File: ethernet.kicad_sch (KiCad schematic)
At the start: 22 parts, among them J2 L834-1G1T-S7, Q2 PMOS_Substrate, U2 LAN8830T_PSA

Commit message: Start of ethernet
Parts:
- removed J2: L834-1G1T-S7, L834-1G1T-S7:BEL_L834-1G1T-S7, symbol Library:L834-1G1T-S7
- removed U2: LAN8830T_PSA, LAN8830T_PSA:QFN50P700X700X100-49N, symbol Library:LAN8830T_PSA
- added J2: ARJM11B1-502-AB-EW2, Library:ABRACON_ARJM11B1-502-AB-EW2, symbol Library:ARJM11B1-502-AB-EW2
- added R11, R12: 100, symbol Device:R_Small_US
- added R2, R6: 75, symbol Device:R_Small_US
- added U2: MXL86110C-AQB-R, QFN40_5X5_MXL, symbol Library:MXL86110C-AQB-R
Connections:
- net ETH_LED1: now also R11.2
- net ETH_LED2: now also R12.2
- net GND: now also J2.12, J2.14, R2.1, R6.1
- new net: J2.11, R11.1
- new net: J2.13, R12.1
- new net: J2.5 (CT), J2.6 (CT__1), R2.2, R6.2
- new net TD1+: J2.1 (TD1+), U2.1 (TPIAP)
- new net TD1-: J2.2 (TD1-), U2.2 (TPIAN)
- new net TD2+: J2.3 (TD2+), U2.4 (TPIBP)
- new net TD2-: J2.4 (TD2-), U2.5 (TPIBN)
- new net TD3+: J2.7 (TD3+), U2.6 (TPICP)
- new net TD3-: J2.8 (TD3-), U2.7 (TPICN)
- new net TD4+: J2.9 (TD4+), U2.9 (TPIDP)
- new net TD4-: J2.10 (TD4-), U2.10 (TPIDN)
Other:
- moved on the sheet: L1, L2

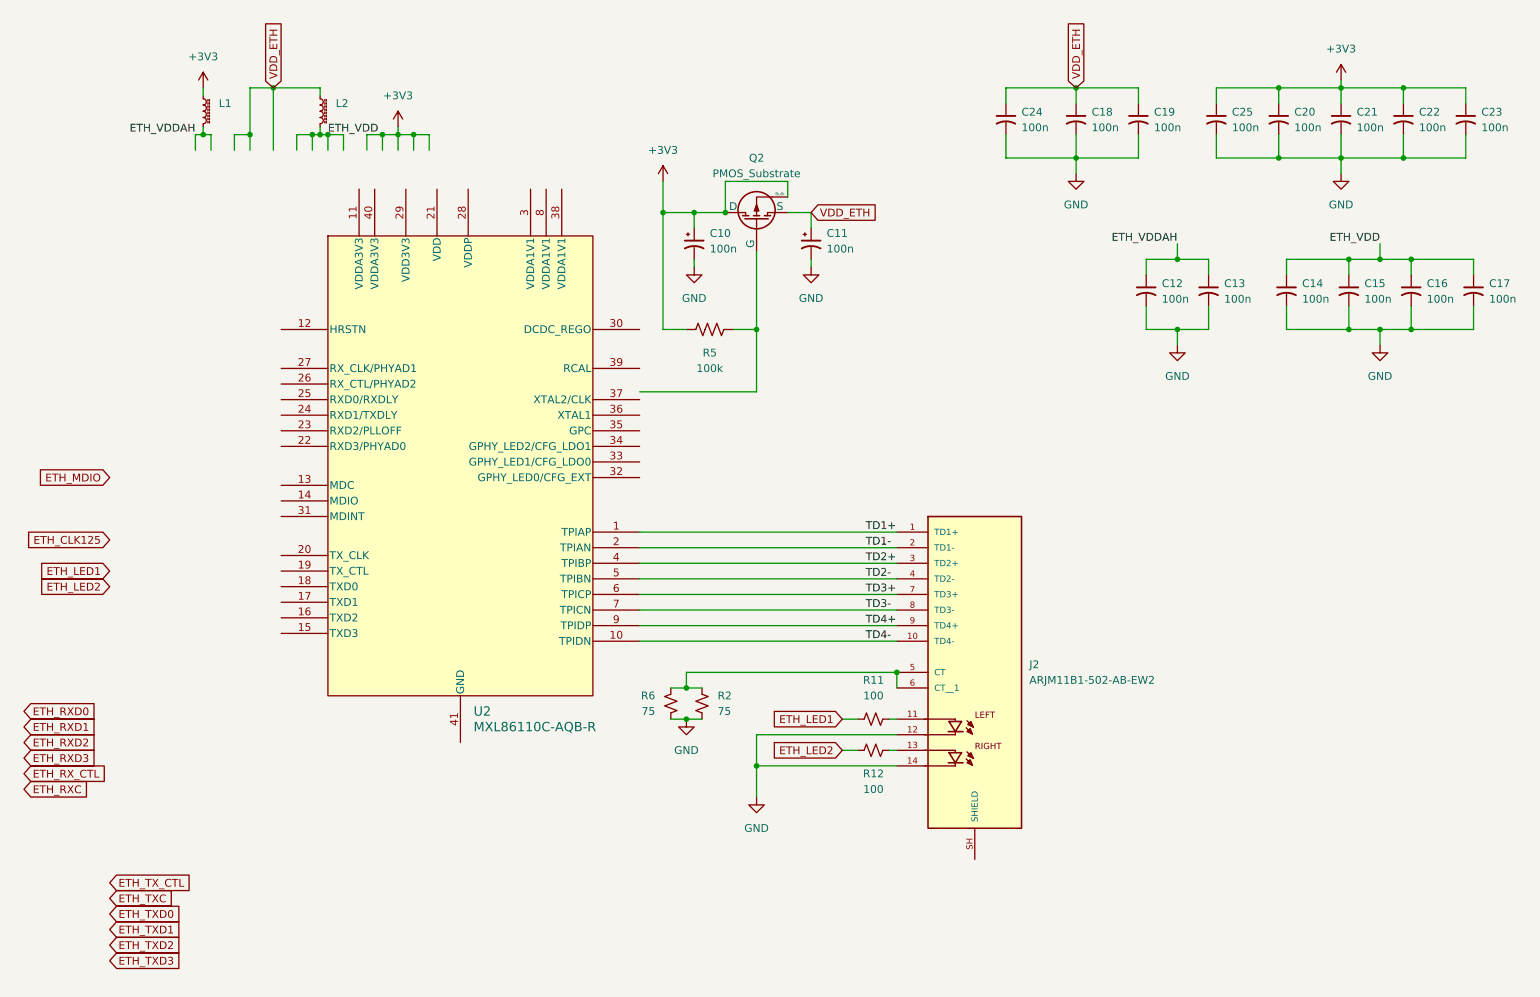
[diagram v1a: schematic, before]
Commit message: Ethernet schematic done
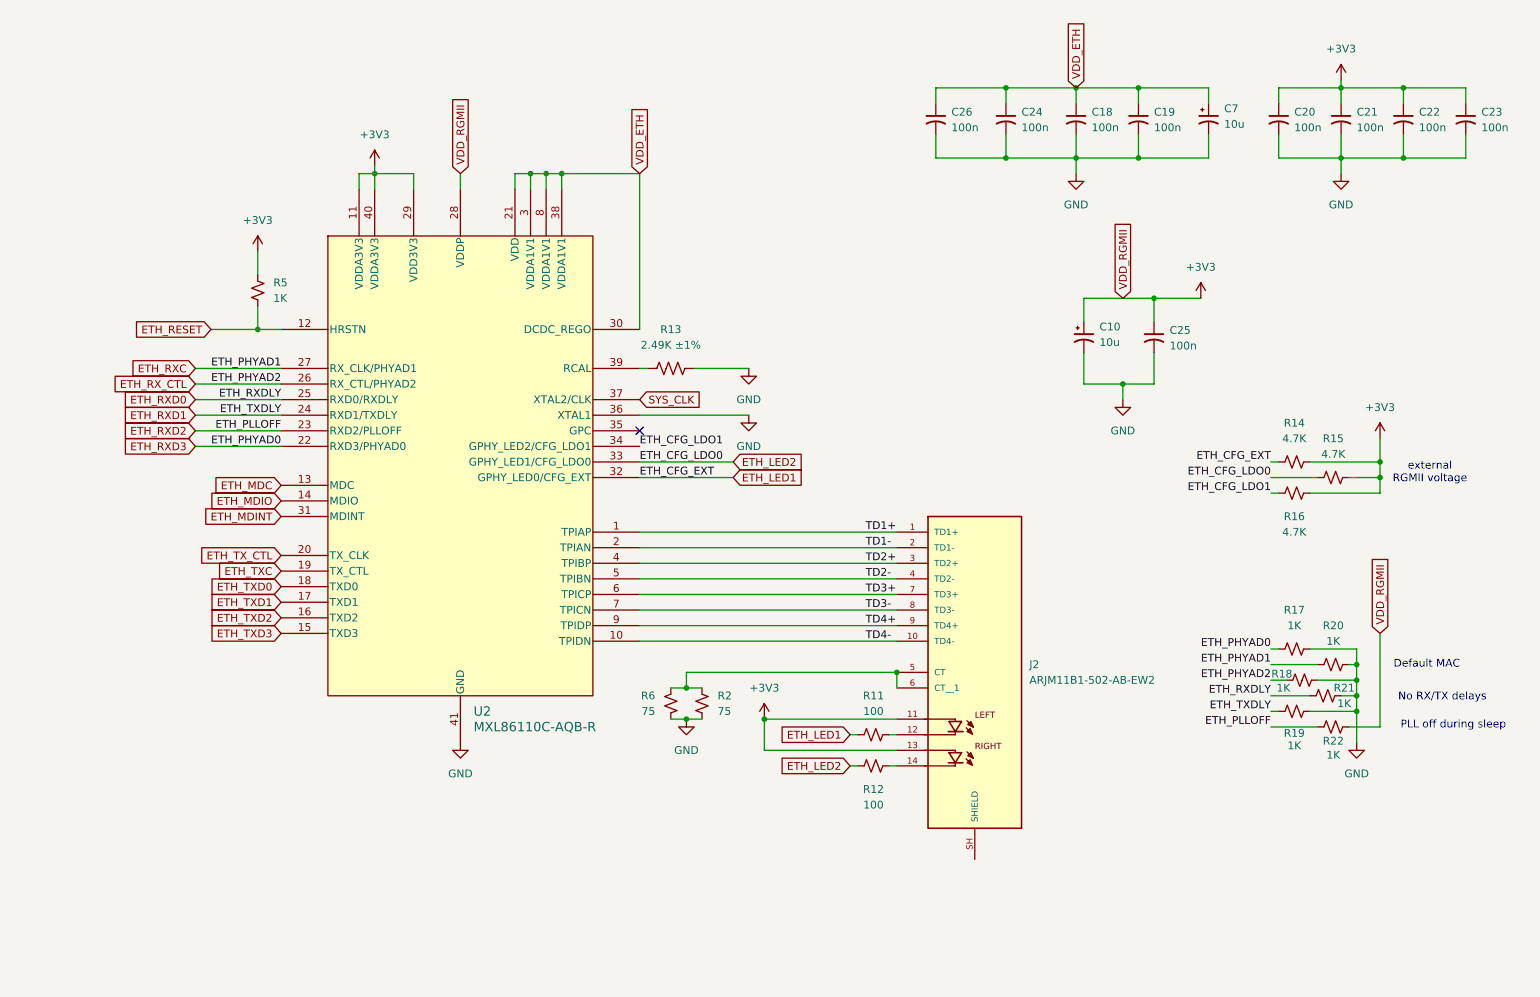
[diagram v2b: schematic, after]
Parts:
- removed C11: 100n, symbol Device:C_Polarized_Small_US
- removed C12, C13, C14, C15, C16, C17: 100n, symbol Device:C_Small_US
- removed L1, L2: L_Ferrite_Small, symbol Device:L_Ferrite_Small
- removed Q2: PMOS_Substrate, symbol Simulation_SPICE:PMOS_Substrate
- removed R5: 100k, symbol Device:R_US
- added C26: 100n, Capacitor_SMD:C_0402_1005Metric, symbol Device:C_Small_US
- added C7: 10u, Capacitor_Tantalum_SMD:CP_EIA-3216-12_Kemet-S, symbol Device:C_Polarized_Small_US
- added R13: 2.49K ±1%, Resistor_SMD:R_0402_1005Metric, symbol Device:R_US
- added R14, R15, R16: 4.7K, Capacitor_SMD:C_0402_1005Metric, symbol Device:R_Small_US
- added R17, R18, R19, R20, R21, R22, R5: 1K, Capacitor_SMD:C_0402_1005Metric, symbol Device:R_Small_US
- C10: value 100n -> 10u; footprint (none) -> Capacitor_Tantalum_SMD:CP_EIA-3216-12_Kemet-S
- C18, C19, C20, C21, C22, C23, C24, C25, R11, R12, R2, R6: footprint (none) -> Capacitor_SMD:C_0402_1005Metric
- U2: footprint QFN40_5X5_MXL -> Library:QFN40_5X5_MXL
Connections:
- net +3V3: now also J2.11, J2.13, U2.11 (VDDA3V3), U2.28 (VDDP), U2.29 (VDD3V3), U2.40 (VDDA3V3), R14.1, R15.1, R16.1, R22.1, R5.2
- net ETH_LED1: now also U2.32 (GPHY_LED0/CFG_EXT), R14.2
- net ETH_LED2: now also U2.33 (GPHY_LED1/CFG_LDO0), R15.2
- net ETH_MDIO: now also U2.14 (MDIO)
- net ETH_RXC: now also U2.27 (RX_CLK/PHYAD1), R20.2
- net ETH_RXD0: now also U2.25 (RXD0/RXDLY), R21.2
- net ETH_RXD1: now also U2.24 (RXD1/TXDLY), R19.2
- net ETH_RXD2: now also U2.23 (RXD2/PLLOFF), R22.2
- net ETH_RXD3: now also U2.22 (RXD3/PHYAD0), R17.2
- net ETH_RX_CTL: now also U2.26 (RX_CTL/PHYAD2), R18.2
- net ETH_TXC: now also U2.19 (TX_CTL)
- net ETH_TXD0: now also U2.18 (TXD0)
- net ETH_TXD1: now also U2.17 (TXD1)
- net ETH_TXD2: now also U2.16 (TXD2)
- net ETH_TXD3: now also U2.15 (TXD3)
- net ETH_TX_CTL: now also U2.20 (TX_CLK)
- net GND: now also U2.36 (XTAL1), U2.41 (GND), C26.2, C7.2, R13.2, R17.1, R18.1, R19.1, R20.1, R21.1; no longer J2.12, J2.14
- net VDD_ETH: now also U2.21 (VDD), U2.3 (VDDA1V1), U2.30 (DCDC_REGO), U2.38 (VDDA1V1), U2.8 (VDDA1V1), C26.1, C7.1
- net at R11.1: now also J2.12; no longer J2.11
- net at R12.1: now also J2.14; no longer J2.13
- net ETH_RESET: now reaches U2.12 (HRSTN)
- net ETH_RESET: now also R5.1
- net ETH_MDC: now reaches U2.13 (MDC)
- net ETH_MDINT: now reaches U2.31 (MDINT)
- net ETH_CFG_LDO1: now reaches U2.34 (GPHY_LED2/CFG_LDO1)
- net ETH_CFG_LDO1: now also R16.2
- net SYS_CLK: now reaches U2.37 (XTAL2/CLK)
- net at U2.39 (RCAL): now also R13.1
- no-connect marks 0 -> 1
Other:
- note added: "Default MAC"
- note added: "No RX/TX delays"
- note added: "PLL off during sleep"
- note added: "external RGMII voltage"

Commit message: Base ethernet signals routed
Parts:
- J2: value ARJM11B1-502-AB-EW2 -> ARJM11D7-502-AB-EW2; footprint Library:ABRACON_ARJM11B1-502-AB-EW2 -> Library:ABRACON_ARJM11D7-502-AB-EW2

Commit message: Etherent MDI rerouted with correct trace widths
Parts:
- J2: value ARJM11D7-502-AB-EW2 -> TMJG0803HENL; footprint Library:ABRACON_ARJM11D7-502-AB-EW2 -> Library:RJ45_TMJG0803HENL
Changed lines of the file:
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@@
 			)
 		)
-		(property "Value" "ARJM11D7-502-AB-EW2"
+		(property "Value" "TMJG0803HENL"
 			(at 204.47 120.6499 0)
 			(show_name no)
@@
 			)
 		)
-		(property "Footprint" "Library:ABRACON_ARJM11D7-502-AB-EW2"
+		(property "Footprint" "Library:RJ45_TMJG0803HENL"
 			(at 195.58 119.38 0)
 			(hide yes)

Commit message: More PHY passives
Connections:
- net +3V3: now also R21.1
- net GND: no longer R21.1
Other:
- note added: "Delay RX CLK"
- note added: "No TX CLK delay"
- note removed: "No RX/TX delays"
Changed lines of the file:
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@@
 		)
 	)
-	(text "PLL off during sleep"
+	(text "No TX CLK delay\n"
 		(exclude_from_sim no)
-		(at 273.558 128.016 0)
+		(at 263.652 125.73 0)
 		(effects
 			(font
 				(size 1.27 1.27)
 			)
-		)
-	)
-	(text "No RX/TX delays"
+			(justify left)
+		)
+	)
+	(text "PLL off during sleep"
 		(exclude_from_sim no)
-		(at 271.78 123.444 0)
+		(at 273.558 128.27 0)
 		(effects
 			(font
 				(size 1.27 1.27)
 			)
+		)
+	)
+	(text "Delay RX CLK"
+		(exclude_from_sim no)
+		(at 263.652 123.19 0)
+		(effects
+			(font
+				(size 1.27 1.27)
+			)
+			(justify left)
 		)
 	)
@@
 	)
 	(junction
+		(at 261.62 123.19)
+		(diameter 0)
+		(color 0 0 0 0)
+	)
+	(junction
 		(at 257.81 118.11)
 		(diameter 0)
@@
 	(junction
 		(at 222.25 24.13)
-		(diameter 0)
-		(color 0 0 0 0)
-	)
-	(junction
-		(at 257.81 123.19)
 		(diameter 0)
 		(color 0 0 0 0)
@@
 	(wire
 		(pts
-			(xy 261.62 128.27) (xy 261.62 113.03)
+			(xy 261.62 128.27) (xy 261.62 123.19)
 		)
 		(stroke
@@
 	(wire
 		(pts
+			(xy 261.62 123.19) (xy 261.62 113.03)
+		)
+		(stroke
+			(width 0)
+			(type default)
+		)
+	)
+	(wire
+		(pts
 			(xy 123.19 38.1) (xy 125.73 38.1)
 		)
@@
 	(wire
 		(pts
-			(xy 257.81 120.65) (xy 257.81 123.19)
-		)
-		(stroke
-			(width 0)
-			(type default)
-		)
-	)
-	(wire
-		(pts
 			(xy 257.81 118.11) (xy 257.81 120.65)
 		)
@@
 	(wire
 		(pts
-			(xy 255.27 123.19) (xy 257.81 123.19)
-		)
-		(stroke
-			(width 0)
-			(type default)
-		)
-	)
-	(wire
-		(pts
 			(xy 243.84 120.65) (xy 246.38 120.65)
 		)
@@
 	(wire
 		(pts
+			(xy 255.27 123.19) (xy 261.62 123.19)
+		)
+		(stroke
+			(width 0)
+			(type default)
+		)
+	)
+	(wire
+		(pts
 			(xy 243.84 85.09) (xy 245.11 85.09)
 		)
@@
 	(wire
 		(pts
-			(xy 257.81 123.19) (xy 257.81 125.73)
-		)
-		(stroke
+			(xy 257.81 120.65) (xy 257.81 125.73)
+		)
+		(stroke

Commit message: More PHY passives
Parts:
- C10, C7: footprint Capacitor_Tantalum_SMD:CP_EIA-3216-12_Kemet-S -> Capacitor_Tantalum_SMD:CP_EIA-2012-12_Kemet-R
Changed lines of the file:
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@@
 			)
 		)
-		(property "Footprint" "Capacitor_Tantalum_SMD:CP_EIA-3216-12_Kemet-S"
+		(property "Footprint" "Capacitor_Tantalum_SMD:CP_EIA-2012-12_Kemet-R"
 			(at 213.36 64.77 0)
 			(hide yes)
@@
 			)
 		)
-		(property "Footprint" "Capacitor_Tantalum_SMD:CP_EIA-3216-12_Kemet-S"
+		(property "Footprint" "Capacitor_Tantalum_SMD:CP_EIA-2012-12_Kemet-R"
 			(at 233.68 29.21 0)
 			(hide yes)

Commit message: PHY RX routing and power
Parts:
- removed C21, C25: 100n, Capacitor_SMD:C_0402_1005Metric, symbol Device:C_Small_US
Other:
- moved on the sheet: C10, C23

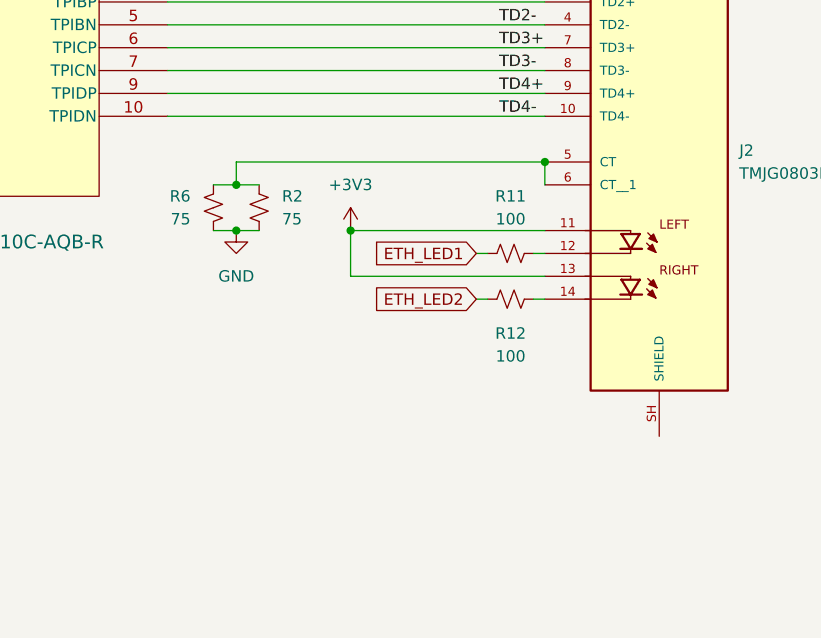
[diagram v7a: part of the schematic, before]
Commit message: Ethernet shielding
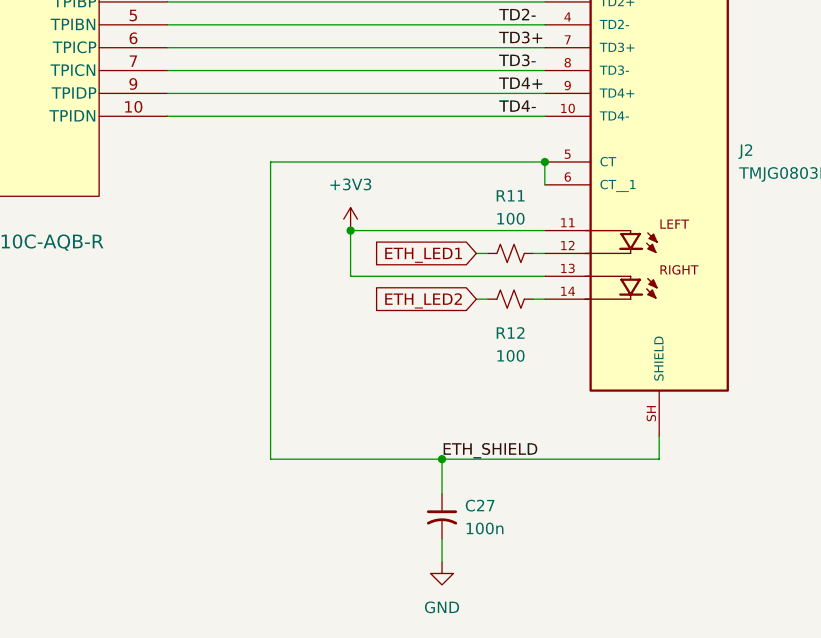
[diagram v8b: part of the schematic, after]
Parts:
- removed R2, R6: 75, Capacitor_SMD:C_0402_1005Metric, symbol Device:R_Small_US
- added C27: 100n, Capacitor_SMD:C_0402_1005Metric, symbol Device:C_Small_US
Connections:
- net GND: now also C27.2
- net ETH_SHIELD: now reaches J2.5 (CT), J2.6 (CT__1)
- net ETH_SHIELD: now also J2.SH (SHIELD), C27.1
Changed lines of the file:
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@@
 	)
 	(junction
-		(at 148.59 127)
-		(diameter 0)
-		(color 0 0 0 0)
-	)
-	(junction
 		(at 257.81 125.73)
 		(diameter 0)
@@
 	)
 	(junction
-		(at 261.62 87.63)
+		(at 171.45 152.4)
 		(diameter 0)
 		(color 0 0 0 0)
 	)
 	(junction
-		(at 148.59 121.92)
+		(at 261.62 87.63)
 		(diameter 0)
 		(color 0 0 0 0)
@@
 	(wire
 		(pts
-			(xy 148.59 127) (xy 151.13 127)
+			(xy 171.45 152.4) (xy 195.58 152.4)
 		)
 		(stroke
@@
 	(wire
 		(pts
+			(xy 152.4 152.4) (xy 152.4 119.38)
+		)
+		(stroke
+			(width 0)
+			(type default)
+		)
+	)
+	(wire
+		(pts
 			(xy 175.26 129.54) (xy 176.53 129.54)
 		)
@@
 	(wire
 		(pts
-			(xy 146.05 121.92) (xy 148.59 121.92)
+			(xy 171.45 163.83) (xy 171.45 161.29)
 		)
 		(stroke
@@
 	(wire
 		(pts
+			(xy 171.45 156.21) (xy 171.45 152.4)
+		)
+		(stroke
+			(width 0)
+			(type default)
+		)
+	)
+	(wire
+		(pts
 			(xy 233.68 26.67) (xy 233.68 24.13)
 		)
@@
 	(wire
 		(pts
+			(xy 152.4 152.4) (xy 171.45 152.4)
+		)
+		(stroke
+			(width 0)
+			(type default)
+		)
+	)
+	(wire
+		(pts
 			(xy 142.24 69.85) (xy 140.97 69.85)
 		)
@@
 	(wire
 		(pts
-			(xy 182.88 119.38) (xy 148.59 119.38)
+			(xy 182.88 119.38) (xy 152.4 119.38)
 		)
 		(stroke
@@
 	(wire
 		(pts
-			(xy 148.59 121.92) (xy 151.13 121.92)
-		)
-		(stroke
-			(width 0)
-			(type default)
-		)
-	)
-	(wire
-		(pts
 			(xy 261.62 85.09) (xy 261.62 81.28)
 		)
@@
 	(wire
 		(pts
-			(xy 148.59 119.38) (xy 148.59 121.92)
+			(xy 195.58 152.4) (xy 195.58 149.86)
 		)
 		(stroke
@@
 		)
 	)
-	(wire
-		(pts
-			(xy 146.05 127) (xy 148.59 127)
-		)
-		(stroke
-			(width 0)
-			(type default)
-		)
-	)
 	(label "VDD_RGMII"
 		(at 111.76 38.1 90)
@@
 		)
 	)
+	(label "ETH_SHIELD"
+		(at 171.45 152.4 0)
+		(effects
+			(font
+				(size 1.27 1.27)
+			)
+			(justify left bottom)
+		)
+	)
 	(label "ETH_PHYAD0"
 		(at 243.84 115.57 180)
@@
 	(symbol
 		(lib_id "power:GND")
-		(at 148.59 127 0)
+		(at 171.45 163.83 0)
 		(unit 1)
 		(body_style 1)
@@
 		(fields_autoplaced yes)
 		(property "Reference" "#PWR06"
-			(at 148.59 133.35 0)
+			(at 171.45 170.18 0)
 			(hide yes)
 			(show_name no)
@@
 		)
 		(property "Value" "GND"
-			(at 148.59 132.08 0)
+			(at 171.45 168.91 0)
 			(show_name no)
 			(do_not_autoplace no)
@@
 		)
 		(property "Footprint" ""
-			(at 148.59 127 0)
+			(at 171.45 163.83 0)
 			(hide yes)
 			(show_name no)
@@
 		)
 		(property "Datasheet" ""
-			(at 148.59 127 0)
+			(at 171.45 163.83 0)
 			(hide yes)
 			(show_name no)
@@
 		)
 		(property "Description" "Power symbol creates a global label with name \"GND\" , ground"
-			(at 148.59 127 0)
+			(at 171.45 163.83 0)
 			(hide yes)
 			(show_name no)
@@
 	(symbol
 		(lib_id "Device:C_Small_US")
+		(at 171.45 158.75 0)
+		(unit 1)
+		(body_style 1)
+		(exclude_from_sim no)
+		(in_bom yes)
+		(on_board yes)
+		(in_pos_files yes)
+		(dnp no)
+		(fields_autoplaced yes)
+		(property "Reference" "C27"
+			(at 173.99 157.6069 0)
+			(show_name no)
+			(do_not_autoplace no)
+			(effects
+				(font
+					(size 1.27 1.27)
+				)
+				(justify left)
+			)
+		)
+		(property "Value" "100n"
+			(at 173.99 160.1469 0)
+			(show_name no)
+			(do_not_autoplace no)
+			(effects
+				(font
+					(size 1.27 1.27)
+				)
+				(justify left)
+			)
+		)
+		(property "Footprint" "Capacitor_SMD:C_0402_1005Metric"
+			(at 171.45 158.75 0)
+			(hide yes)
+			(show_name no)
+			(do_not_autoplace no)
+			(effects
+				(font
+					(size 1.27 1.27)
+				)
+			)
+		)
+		(property "Datasheet" ""
+			(at 171.45 158.75 0)
+			(hide yes)
+			(show_name no)
+			(do_not_autoplace no)
+			(effects
+				(font
+					(size 1.27 1.27)
+				)
+			)
+		)
+		(property "Description" "capacitor, small US symbol"
+			(at 171.45 158.75 0)
+			(hide yes)
+			(show_name no)
+			(do_not_autoplace no)
+			(effects
+				(font
+					(size 1.27 1.27)
+				)
+			)
+		)
+		(pin "2"
+		)
+		(pin "1"
+		)
+		(instances
+			(project "little-witch"
+				(path "/ff2e066b-bdbd-49a5-9475-b60d81b3cdf5"
+					(reference "C27")
+					(unit 1)
+				)
+			)
+		)
+	)
+	(symbol
+		(lib_id "Device:C_Small_US")
 		(at 222.25 29.21 0)
 		(unit 1)
@@
 					(unit 1)
 				)
-			)
-		)
-	)
-	(symbol
-		(lib_id "Device:R_Small_US")
-		(at 146.05 124.46 0)
-		(mirror x)
-		(unit 1)
-		(body_style 1)
-		(exclude_from_sim no)
-		(in_bom yes)
-		(on_board yes)
-		(in_pos_files yes)
-		(dnp no)
-		(property "Reference" "R6"
-			(at 143.51 123.1899 0)
-			(show_name no)
-			(do_not_autoplace no)
-			(effects
-				(font
-					(size 1.27 1.27)
-				)
-				(justify right)
-			)
-		)
-		(property "Value" "75"
-			(at 143.51 125.7299 0)
-			(show_name no)
-			(do_not_autoplace no)
-			(effects
-				(font
-					(size 1.27 1.27)
-				)
-				(justify right)
-			)
-		)
-		(property "Footprint" "Capacitor_SMD:C_0402_1005Metric"
-			(at 146.05 124.46 0)
-			(hide yes)
-			(show_name no)
-			(do_not_autoplace no)
-			(effects
-				(font
-					(size 1.27 1.27)
-				)
-			)
-		)
-		(property "Datasheet" ""
-			(at 146.05 124.46 0)
-			(hide yes)
-			(show_name no)
-			(do_not_autoplace no)
-			(effects
-				(font
-					(size 1.27 1.27)
-				)
-			)
-		)
-		(property "Description" "Resistor, small US symbol"
-			(at 146.05 124.46 0)
-			(hide yes)
-			(show_name no)
-			(do_not_autoplace no)
-			(effects
-				(font
-					(size 1.27 1.27)
-				)
-			)
-		)
-		(pin "1"
-		)
-		(pin "2"
-		)
-		(instances
-			(project "little-witch"
-				(path "/ff2e066b-bdbd-49a5-9475-b60d81b3cdf5"
-					(reference "R6")
-					(unit 1)
-				)
-			)
-		)
-	)
-	(symbol
-		(lib_id "Device:R_Small_US")
-		(at 151.13 124.46 180)
-		(unit 1)
-		(body_style 1)
-		(exclude_from_sim no)
-		(in_bom yes)
-		(on_board yes)
-		(in_pos_files yes)
-		(dnp no)
-		(fields_autoplaced yes)
-		(property "Reference" "R2"
-			(at 153.67 123.1899 0)
-			(show_name no)
-			(do_not_autoplace no)
-			(effects
-				(font
-					(size 1.27 1.27)
-				)
-				(justify right)
-			)
-		)
-		(property "Value" "75"
-			(at 153.67 125.7299 0)
-			(show_name no)
-			(do_not_autoplace no)
-			(effects
-				(font
-					(size 1.27 1.27)
-				)
-				(justify right)
-			)
-		)
-		(property "Footprint" "Capacitor_SMD:C_0402_1005Metric"
-			(at 151.13 124.46 0)
-			(hide yes)
-			(show_name no)
-			(do_not_autoplace no)
-			(effects
-				(font
-					(size 1.27 1.27)
-				)
-			)
-		)
-		(property "Datasheet" ""
-			(at 151.13 124.46 0)
-			(hide yes)
-			(show_name no)
-			(do_not_autoplace no)
-			(effects
-				(font
-					(size 1.27 1.27)
-				)
-			)
-		)
-		(property "Description" "Resistor, small US symbol"
-			(at 151.13 124.46 0)
-			(hide yes)
-			(show_name no)
-			(do_not_autoplace no)
-			(effects
-				(font
-					(size 1.27 1.27)
-				)
-			)
-		)
-		(pin "1"
-		)
-		(pin "2"
-		)
-		(instances
-			(project "little-witch"
-				(path "/ff2e066b-bdbd-49a5-9475-b60d81b3cdf5"
-					(reference "R2")
-					(unit 1)
-				)
